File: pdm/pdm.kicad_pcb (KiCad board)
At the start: 2 copper layers, 100 x 100 mm, 87 parts, among them J1 Conn_01x05, J2 Conn_01x04_Male, U1 AZ1117CH-3_3TRG1, U10 BTS443P, U11 TLP291, U12 BTS443P, U13 TLP291, U2 SN65HVD233, U3 STM32F103C8Tx, U4 BTS443P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

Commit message: small changes
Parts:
- moved C10 1.79 mm to (145.5, 108.2), turned to 270 degrees
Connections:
- net /PD0 renamed /OSC_N
- net /PD1 renamed /OSC_P
- net Net-(J2-Pad2) renamed /_N
- net Net-(J2-Pad3) renamed /_P
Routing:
- net +3V3: track 48.1 -> 121.8 mm, vias 6 -> 11
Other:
- board text added: "BLOCK1"
- board text added: "BLOCK2"
- board text added: "BLOCK3"
- board text added: "BLOCK4"
- board text added: "BLOCK5"

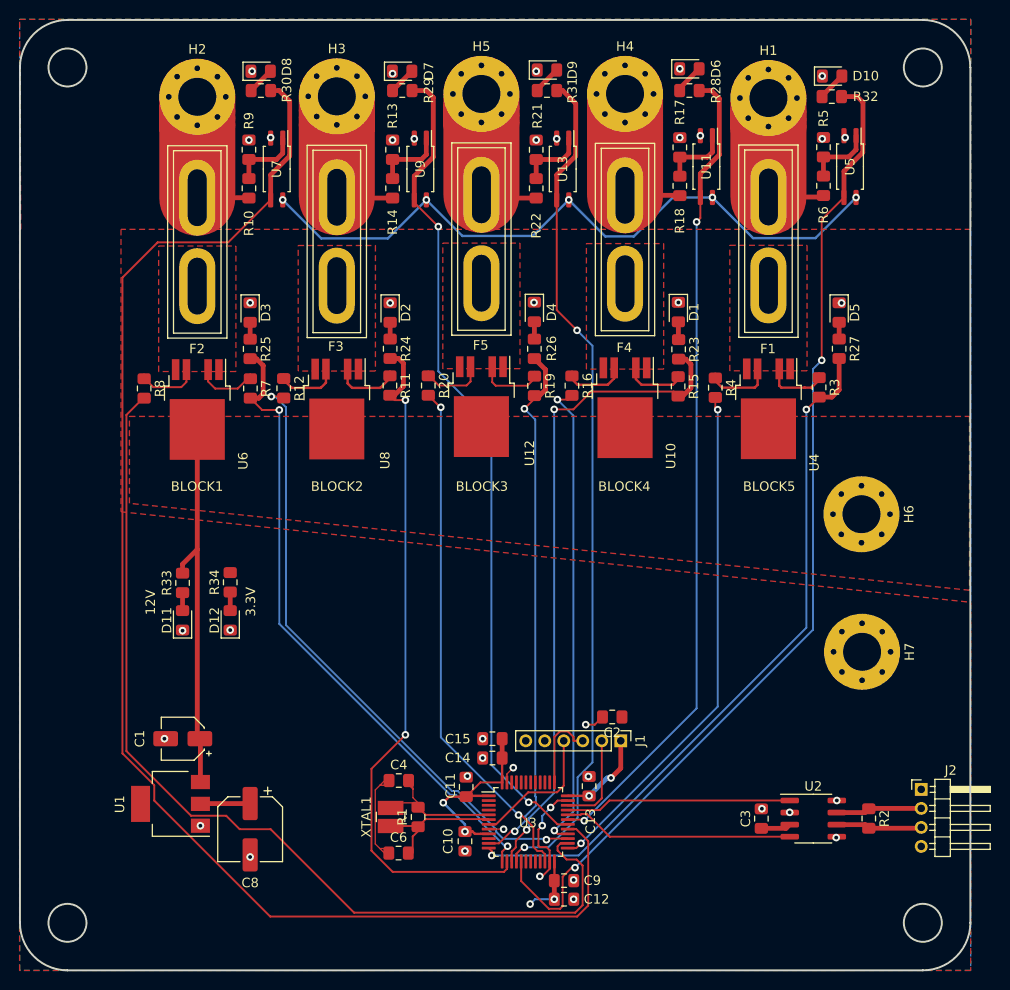
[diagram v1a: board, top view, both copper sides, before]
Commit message: layout duplication
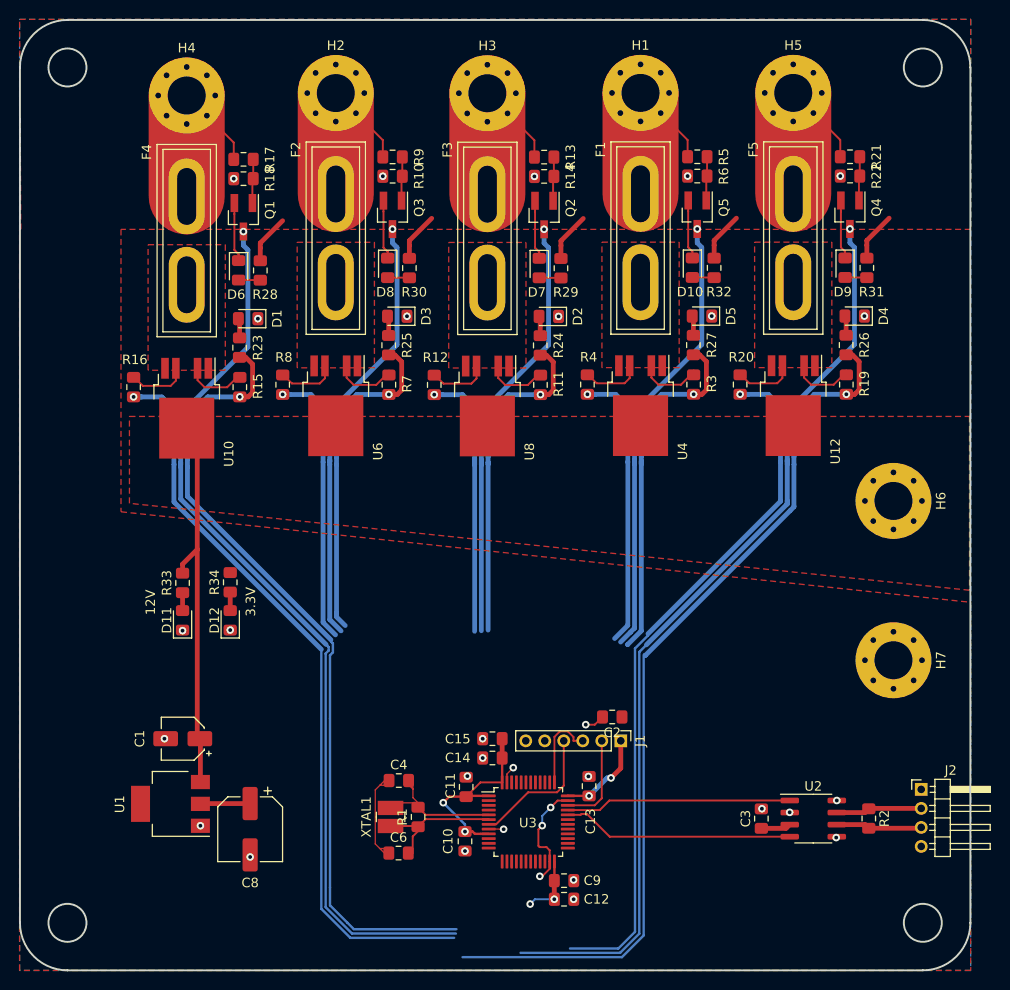
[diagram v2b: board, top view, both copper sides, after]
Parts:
- removed U11, U13, U5, U7, U9: TLP291, Package_SO:SOIC-4_4.55x2.6mm_P1.27mm
- added Q1: Q_NPN_BCE, Package_TO_SOT_SMD:SOT-23_Handsoldering, F.Cu at (122.2, 42.5)
- added Q2: Q_NPN_BCE, Package_TO_SOT_SMD:SOT-23_Handsoldering, F.Cu at (153.9, 42.3)
- added Q3: Q_NPN_BCE, Package_TO_SOT_SMD:SOT-23_Handsoldering, F.Cu at (137.9, 42.3)
- added Q4: Q_NPN_BCE, Package_TO_SOT_SMD:SOT-23_Handsoldering, F.Cu at (186.0, 42.3)
- added Q5: Q_NPN_BCE, Package_TO_SOT_SMD:SOT-23_Handsoldering, F.Cu at (170.0, 42.3)
- moved D6 52.0 mm to (121.7, 48.1), turned to 270 degrees
- moved R28 49.0 mm to (124.0, 48.1), turned to 270 degrees
- moved R23 46.2 mm to (121.8, 56.3)
- moved H4 46.1 mm to (116.3, 29.7)
- moved R16 46.1 mm to (110.7, 60.4)
- moved F4 46.1 mm to (116.3, 40.4)
- moved R15 46.1 mm to (121.8, 60.4)
- moved U10 46.1 mm to (116.3, 62.6)
- moved R17 45.9 mm to (122.2, 36.4), turned to 180 degrees
- moved R18 45.9 mm to (122.2, 38.5), turned to 180 degrees
- moved D1 45.3 mm to (122.7, 53.2), turned to 180 degrees
- moved R31 38.5 mm to (187.8, 47.9), turned to 270 degrees
- moved D9 37.6 mm to (185.5, 47.9), turned to 270 degrees
- moved D4 33.7 mm to (186.5, 52.9), turned to 180 degrees
- moved R22 33.0 mm to (186.1, 38.2), turned to 180 degrees
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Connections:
- D10 pad 1: GND -> Net-(D10-Pad1)
- D6 pad 1: GND -> Net-(D6-Pad1)
- D7 pad 1: GND -> Net-(D7-Pad1)
- D8 pad 1: GND -> Net-(D8-Pad1)
- D9 pad 1: GND -> Net-(D9-Pad1)
- R10 pad 1: /sheet5F955F69/vload -> Net-(Q3-Pad1)
- R10 pad 2: Net-(R10-Pad2) -> GND
- R13 pad 1: Net-(R13-Pad1) -> Net-(Q2-Pad1)
- R13 pad 2: GND -> /sheet5F95602F/vload
- R14 pad 1: /sheet5F95602F/vload -> Net-(Q2-Pad1)
- R14 pad 2: Net-(R13-Pad1) -> GND
- R17 pad 1: Net-(R17-Pad1) -> Net-(Q1-Pad1)
- R17 pad 2: GND -> /sheet5F9560CD/vload
- R18 pad 1: /sheet5F9560CD/vload -> Net-(Q1-Pad1)
- R18 pad 2: Net-(R17-Pad1) -> GND
- R21 pad 1: Net-(R21-Pad1) -> Net-(Q4-Pad1)
- R21 pad 2: GND -> /fuse_block/vload
- R22 pad 1: /fuse_block/vload -> Net-(Q4-Pad1)
- R22 pad 2: Net-(R21-Pad1) -> GND
- R28 pad 1: Net-(D6-Pad2) -> +3V3
- R28 pad 2: /fuse5 -> Net-(D6-Pad2)
- R29 pad 1: Net-(D7-Pad2) -> +3V3
- R29 pad 2: /fuse4 -> Net-(D7-Pad2)
- R30 pad 1: Net-(D8-Pad2) -> +3V3
- R30 pad 2: /fuse3 -> Net-(D8-Pad2)
- R31 pad 1: Net-(D9-Pad2) -> +3V3
- R31 pad 2: /fuse1 -> Net-(D9-Pad2)
- R32 pad 1: Net-(D10-Pad2) -> +3V3
- R32 pad 2: /fuse2 -> Net-(D10-Pad2)
- R5 pad 1: Net-(R5-Pad1) -> Net-(Q5-Pad1)
- R5 pad 2: GND -> /sheet5F955EDF/vload
- R6 pad 1: /sheet5F955EDF/vload -> Net-(Q5-Pad1)
- R6 pad 2: Net-(R5-Pad1) -> GND
- R9 pad 1: Net-(R10-Pad2) -> Net-(Q3-Pad1)
- R9 pad 2: GND -> /sheet5F955F69/vload
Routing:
- net /fuse3: track 149.7 -> 46.1 mm, vias 0 -> 1
- net /sense3: track 102.5 -> 29.3 mm, vias 0 -> 1
- net /fuse2: track 108.1 -> 47.4 mm, vias 2 -> 1
- net +3V3: track 121.8 -> 74.1 mm, vias 11 -> 6
- net /fuse4: track 87.6 -> 46.0 mm, vias 2 -> 1
- net /act1: track 56.1 -> 93.7 mm, vias 2 -> 1
- net /act4: track 72.6 -> 35.5 mm, vias 2 -> 1
- net /act2: track 74.5 -> 37.7 mm, vias 2 -> 1
- net /sense4: track 65.5 -> 29.0 mm, vias 2 -> 1
- net /act3: track 68.0 -> 35.1 mm, vias 2 -> 1
- net /sense5: track 50.1 -> 79.0 mm, vias 2 -> 1
- net /sense2: track 54.6 -> 29.8 mm, vias 2 -> 1
- net /sense1: track 54.6 -> 74.0 mm, vias 2 -> 1
- net /act5: track 69.2 -> 84.8 mm, vias 2 -> 1
- net /fuse5: track 86.1 -> 95.8 mm, vias 2 -> 1
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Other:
- board text removed: "BLOCK1"
- board text removed: "BLOCK2"
- board text removed: "BLOCK3"
- board text removed: "BLOCK4"
- board text removed: "BLOCK5"

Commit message: FUCK MANUAL ROUTING
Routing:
- net /sense2: track 29.8 -> 89.5 mm, vias 1 -> 2
- net /fuse2: track 47.4 -> 105.1 mm, vias 1 -> 2
- net /act2: track 37.7 -> 84.5 mm, vias 1 -> 2
- net /fuse3: track 46.1 -> 90.0 mm, vias 1 -> 2
- net /sense3: track 29.3 -> 70.5 mm, vias 1 -> 2
- net /act3: track 35.1 -> 60.4 mm, vias 1 -> 2
- net /sense4: track 29.0 -> 54.0 mm, vias 1 -> 2
- net /fuse4: track 46.0 -> 70.1 mm, vias 1 -> 2
- net /sense5: track 79.0 -> 102.3 mm
- net /act4: track 35.5 -> 56.3 mm, vias 1 -> 2
- net /act1: track 93.7 -> 76.7 mm, vias 1 -> 2
- net /act5: track 84.8 -> 70.7 mm, vias 1 -> 2
- net /sense1: track 74.0 -> 60.9 mm, vias 1 -> 2
- net GND: track 18.9 -> 27.8 mm, vias 32 -> 31
- net (no net): track 0.00 -> 8.23 mm, vias 0 -> 2
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
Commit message: better routing
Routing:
- net /fuse5: track 102.0 -> 140.9 mm, vias 2 -> 0
- net /sense2: track 89.5 -> 51.4 mm
- net +3V3: track 74.6 -> 52.8 mm, vias 6 -> 1
- net /fuse1: track 102.8 -> 87.2 mm
- net /fuse2: track 105.1 -> 90.0 mm
- net GND: track 27.8 -> 13.1 mm
- net /act2: track 84.5 -> 74.8 mm
- net (no net): track 8.23 -> 0.00 mm, vias 2 -> 0
- net /fuse3: track 90.0 -> 84.0 mm
- net /act4: track 56.3 -> 62.2 mm
- net /act1: track 76.7 -> 80.8 mm
- net /fuse4: track 70.1 -> 67.9 mm
- net /sense3: track 70.5 -> 68.8 mm
- net /sense5: track 102.3 -> 101.3 mm, vias 1 -> 0
- net /sense1: track 60.9 -> 61.7 mm

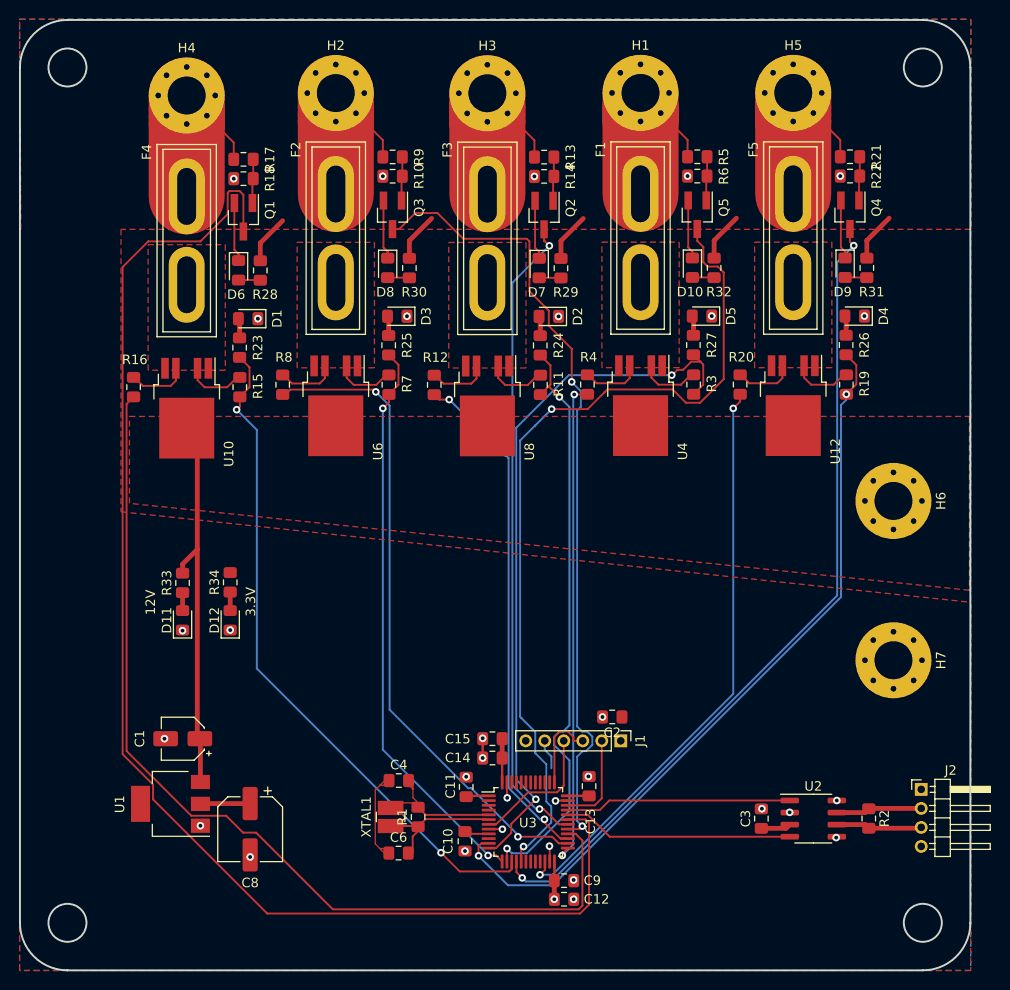
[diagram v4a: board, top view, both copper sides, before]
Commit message: replaced with stm32f042
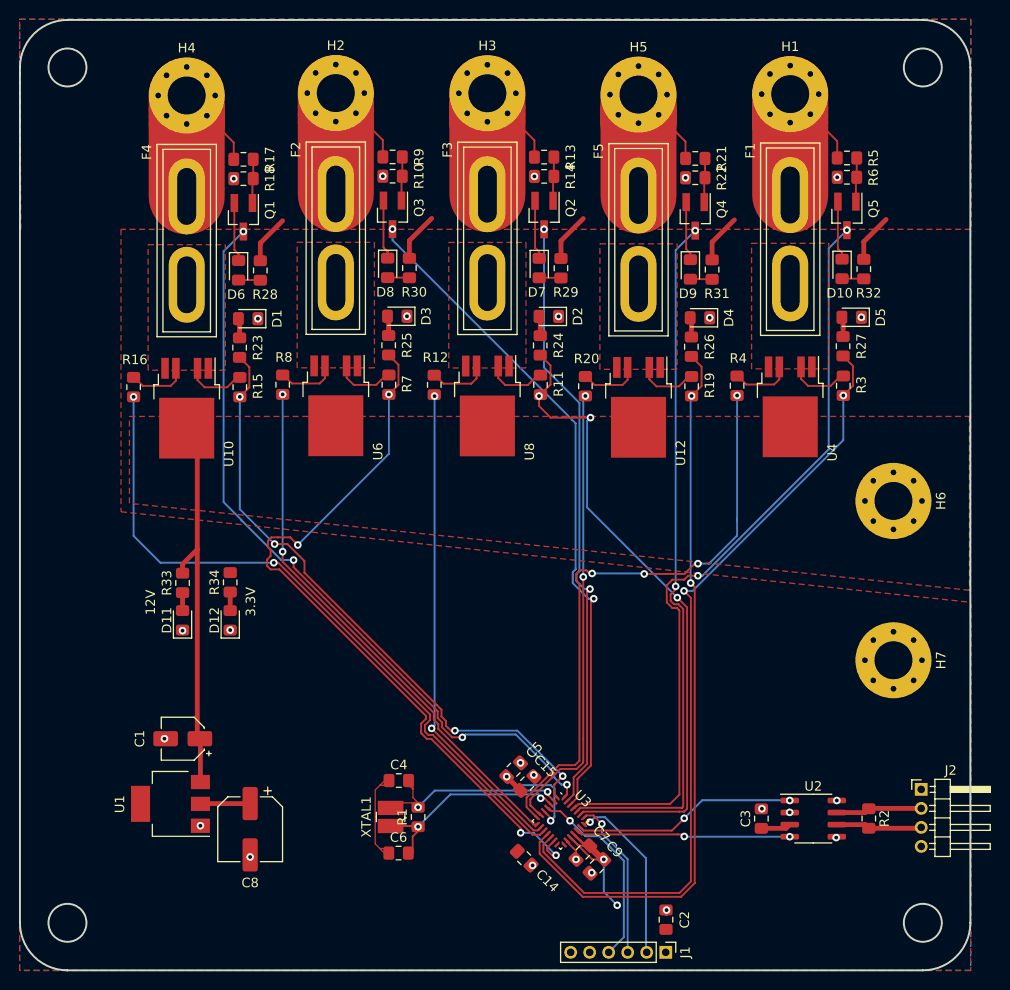
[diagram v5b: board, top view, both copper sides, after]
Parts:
- removed C10, C11, C12, C13: 10nF, Capacitor_SMD:C_0805_2012Metric_Pad1.15x1.40mm_HandSolder
- added C5: 100nF, Capacitor_SMD:C_0805_2012Metric_Pad1.15x1.40mm_HandSolder, F.Cu at (150.7, 100.7)
- added C7: 100nF, Capacitor_SMD:C_0805_2012Metric_Pad1.15x1.40mm_HandSolder, F.Cu at (158.0, 109.4)
- C9: value 10nF -> 100nF
- U3: value STM32F103C8Tx -> STM32F042G6Ux; footprint Package_QFP:LQFP-48_7x7mm_P0.5mm -> Package_DFN_QFN:QFN-28_4x4mm_P0.5mm
- moved J1 22.8 mm to (166.7, 119.9)
- moved C2 22.1 mm to (166.7, 116.5), turned to 90 degrees
- moved R19 16.3 mm to (169.4, 60.3)
- moved R21 16.3 mm to (169.8, 36.4)
- moved R22 16.3 mm to (169.8, 38.4)
- moved R26 16.3 mm to (169.4, 56.2)
- moved D4 16.3 mm to (170.3, 53.1)
- moved D9 16.3 mm to (169.3, 48.0)
- moved F5 16.3 mm to (163.8, 40.3)
- moved H5 16.3 mm to (163.8, 29.6)
- moved Q4 16.3 mm to (169.8, 42.5)
- moved R20 16.3 mm to (158.2, 60.3)
- moved R31 16.3 mm to (171.5, 48.0)
- moved U12 16.3 mm to (163.8, 62.5)
- moved R27 15.7 mm to (185.3, 56.1)
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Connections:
- U3 pad 1: +3V3 -> /act5
- U3 pad 10: (no net) -> /sense5
- U3 pad 14: /act4 -> (no net)
- U3 pad 15: /act5 -> (no net)
- U3 pad 16: /fuse1 -> GND
- U3 pad 17: /fuse2 -> +3V3
- U3 pad 18: (no net) -> +3V3
- U3 pad 19: (no net) -> /canrx
- U3 pad 2: (no net) -> /OSC_N
- U3 pad 20: (no net) -> /cantx
- U3 pad 21: (no net) -> /SWDIO
- U3 pad 22: /sense1 -> /SWCLK
- U3 pad 23: GND -> /act4
- U3 pad 24: +3V3 -> /fuse1
- U3 pad 25: /sense2 -> /fuse2
- U3 pad 26: /sense3 -> /fuse3
- U3 pad 27: /sense4 -> /fuse4
- U3 pad 28: /sense5 -> /fuse5
- U3 pad 3: (no net) -> /OSC_P
- U3 pad 4: (no net) -> /NRST
- U3 pad 5: /OSC_N -> +3V3
- U3 pad 6: /OSC_P -> /sense1
- U3 pad 7: /NRST -> /sense2
- U3 pad 8: GND -> /sense3
- U3 pad 9: +3V3 -> /sense4
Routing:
- net /fuse5: track 140.9 -> 81.0 mm, vias 0 -> 4
- net /sense5: track 101.3 -> 72.8 mm, vias 0 -> 2
- net /act3: track 60.1 -> 79.0 mm, vias 2 -> 4
- net +3V3: track 52.8 -> 67.6 mm, vias 1 -> 4
- net /sense1: track 61.7 -> 48.0 mm
- net /fuse1: track 87.2 -> 73.9 mm
- net /fuse3: track 84.0 -> 70.9 mm
- net /sense3: track 68.8 -> 56.6 mm
- net /sense2: track 51.4 -> 63.2 mm, vias 2 -> 4
- net /act2: track 74.8 -> 83.6 mm
- net /fuse2: track 90.0 -> 81.4 mm
- net /SWDIO: track 9.92 -> 18.5 mm, vias 0 -> 1
- net GND: track 13.1 -> 4.55 mm, vias 31 -> 25
- net /SWCLK: track 8.67 -> 17.0 mm, vias 0 -> 1
- net /OSC_P: track 14.3 -> 22.5 mm, vias 0 -> 2
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
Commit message: neatened up traces
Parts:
- J1: footprint Connector_PinHeader_2.00mm:PinHeader_1x06_P2.00mm_Vertical -> Connector_PinHeader_2.00mm:PinHeader_1x05_P2.00mm_Vertical
- moved C2 5.17 mm to (171.4, 118.5), turned to 0 degrees
- moved C3 3.94 mm to (172.8, 105.7)
- moved R2 3.94 mm to (184.1, 105.7)
- moved U2 3.94 mm to (178.3, 105.7)
- moved J1 1.40 mm to (166.7, 118.5)
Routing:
- net /fuse3: track 70.9 -> 99.1 mm
- net /sense1: track 48.0 -> 73.6 mm
- net /sense4: track 51.3 -> 72.8 mm, vias 2 -> 4
- net /fuse4: track 63.8 -> 84.7 mm
- net /fuse2: track 81.4 -> 92.2 mm
- net /sense2: track 63.2 -> 72.9 mm, vias 4 -> 2
- net /act3: track 79.0 -> 86.6 mm
- net /act2: track 83.6 -> 89.4 mm
- net /act4: track 69.2 -> 74.7 mm
- net /_N: track 9.07 -> 13.1 mm
- net /_P: track 9.08 -> 13.1 mm
- net /canrx: track 22.7 -> 19.1 mm
- net /act1: track 77.3 -> 74.9 mm
- net GND: track 4.55 -> 6.77 mm, vias 25 -> 24
- net /act5: track 66.6 -> 68.3 mm
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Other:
- board text added: "12V - 3.3V LVR"
- board text added: "3V3"
- board text added: "CAN Transceiver"
- board text added: "CANH"
- board text added: "CANL"
- board text added: "GND"
- board text added: "NRST"
- board text added: "STM32F042"
- board text added: "SWCLK"
- board text added: "SWDIO"

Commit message: more neatening
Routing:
- net /act5: track 68.3 -> 69.1 mm
